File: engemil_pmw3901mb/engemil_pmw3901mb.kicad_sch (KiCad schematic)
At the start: 20 parts, among them J1 6130XX11121, U1 PMW3901MB-TXQT, U2 TPD8E003DQDR, U3 LM66100QDCKRQ1, U4 TLV77318PDBVR

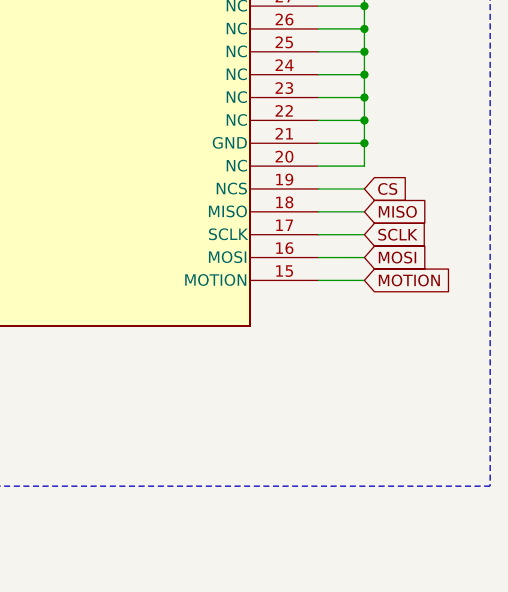
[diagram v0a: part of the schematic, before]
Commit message: - Finalized version 2 - Updated PCB pdf file - Updated README - Updated images - Updated PCB design - Updated gerber files
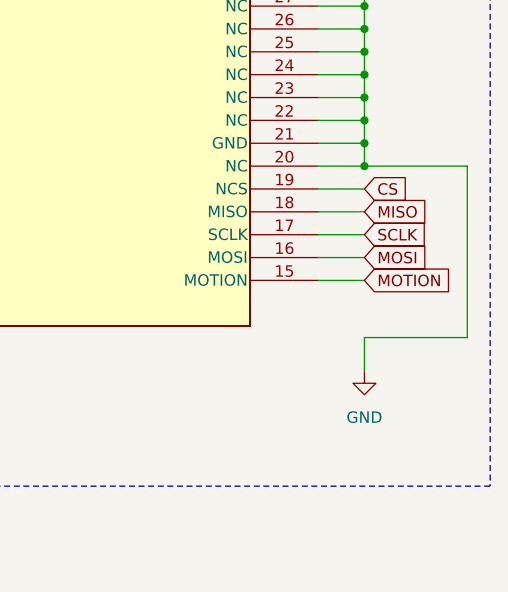
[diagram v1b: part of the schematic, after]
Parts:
- C1, C2: footprint engemil_pmw3901mb_module_footprint_library:C0805 -> CAPC2012X110N
- C3, C4, C7, C9: footprint C0805 -> CAPC2012X110N
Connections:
- net GND: now also U1.1 (GND), U1.20 (NC), U1.21 (GND), U1.22 (NC), U1.23 (NC), U1.24 (NC), U1.25 (NC), U1.26 (NC), U1.27 (NC), U1.28 (NC), U1.29 (GND)
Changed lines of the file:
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@@
 	)
 	(junction
+		(at 266.7 88.9)
+		(diameter 0)
+		(color 0 0 0 0)
+	)
+	(junction
 		(at 191.77 34.29)
 		(diameter 0)
@@
 	(wire
 		(pts
+			(xy 278.13 88.9) (xy 278.13 107.95)
+		)
+		(stroke
+			(width 0)
+			(type default)
+		)
+	)
+	(wire
+		(pts
 			(xy 205.74 88.9) (xy 205.74 91.44)
 		)
@@
 	(wire
 		(pts
+			(xy 266.7 88.9) (xy 278.13 88.9)
+		)
+		(stroke
+			(width 0)
+			(type default)
+		)
+	)
+	(wire
+		(pts
 			(xy 135.89 76.2) (xy 135.89 71.12)
 		)
@@
 	(wire
 		(pts
+			(xy 266.7 107.95) (xy 266.7 111.76)
+		)
+		(stroke
+			(width 0)
+			(type default)
+		)
+	)
+	(wire
+		(pts
 			(xy 266.7 68.58) (xy 266.7 71.12)
 		)
@@
 	(wire
 		(pts
+			(xy 278.13 107.95) (xy 266.7 107.95)
+		)
+		(stroke
+			(width 0)
+			(type default)
+		)
+	)
+	(wire
+		(pts
 			(xy 82.55 105.41) (xy 39.37 105.41)
 		)
@@
 	)
 	(symbol
+		(lib_id "power:GND")
+		(at 266.7 111.76 0)
+		(unit 1)
+		(exclude_from_sim no)
+		(in_bom yes)
+		(on_board yes)
+		(dnp no)
+		(fields_autoplaced yes)
+		(property "Reference" "#PWR023"
+			(at 266.7 118.11 0)
+			(effects
+				(font
+					(size 1.27 1.27)
+				)
+				(hide yes)
+			)
+		)
+		(property "Value" "GND"
+			(at 266.7 116.84 0)
+			(effects
+				(font
+					(size 1.27 1.27)
+				)
+			)
+		)
+		(property "Footprint" ""
+			(at 266.7 111.76 0)
+			(effects
+				(font
+					(size 1.27 1.27)
+				)
+				(hide yes)
+			)
+		)
+		(property "Datasheet" ""
+			(at 266.7 111.76 0)
+			(effects
+				(font
+					(size 1.27 1.27)
+				)
+				(hide yes)
+			)
+		)
+		(property "Description" "Power symbol creates a global label with name \"GND\" , ground"
+			(at 266.7 111.76 0)
+			(effects
+				(font
+					(size 1.27 1.27)
+				)
+				(hide yes)
+			)
+		)
+		(pin "1"
+		)
+		(instances
+			(project "engemil_pmw3901mb"
+				(path "/4b3d6c6d-c090-43d6-aef4-73c7c564178d"
+					(reference "#PWR023")
+					(unit 1)
+				)
+			)
+		)
+	)
+	(symbol
 		(lib_id "engemil_pmw3901mb_module_symbol_library:C0805C106K4PAC7210")
 		(at 121.92 76.2 270)
@@
 			)
 		)
-		(property "Footprint" "C0805"
+		(property "Footprint" "CAPC2012X110N"
 			(at 25.73 85.09 0)
 			(effects
@@
 			)
 		)
-		(property "Footprint" "C0805"
+		(property "Footprint" "CAPC2012X110N"
 			(at 56.21 48.26 0)
 			(effects
@@
 			)
 		)
-		(property "Footprint" "engemil_pmw3901mb_module_footprint_library:C0805"
+		(property "Footprint" "CAPC2012X110N"
 			(at 186.36 91.44 0)
 			(effects
@@
 			)
 		)
-		(property "Footprint" "engemil_pmw3901mb_module_footprint_library:C0805"
+		(property "Footprint" "CAPC2012X110N"
 			(at 122.86 91.44 0)
 			(effects
@@
 			)
 		)
-		(property "Footprint" "C0805"
+		(property "Footprint" "CAPC2012X110N"
 			(at 62.56 87.63 0)
 			(effects
@@
 			)
 		)
-		(property "Footprint" "C0805"
+		(property "Footprint" "CAPC2012X110N"
 			(at 73.99 48.26 0)
 			(effects
